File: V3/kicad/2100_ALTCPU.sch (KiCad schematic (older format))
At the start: 24 parts, among them U2100 Z8-L180-S180-180-PQFP-80, U2101 GAL16V8, X2100 14.7456 MHz

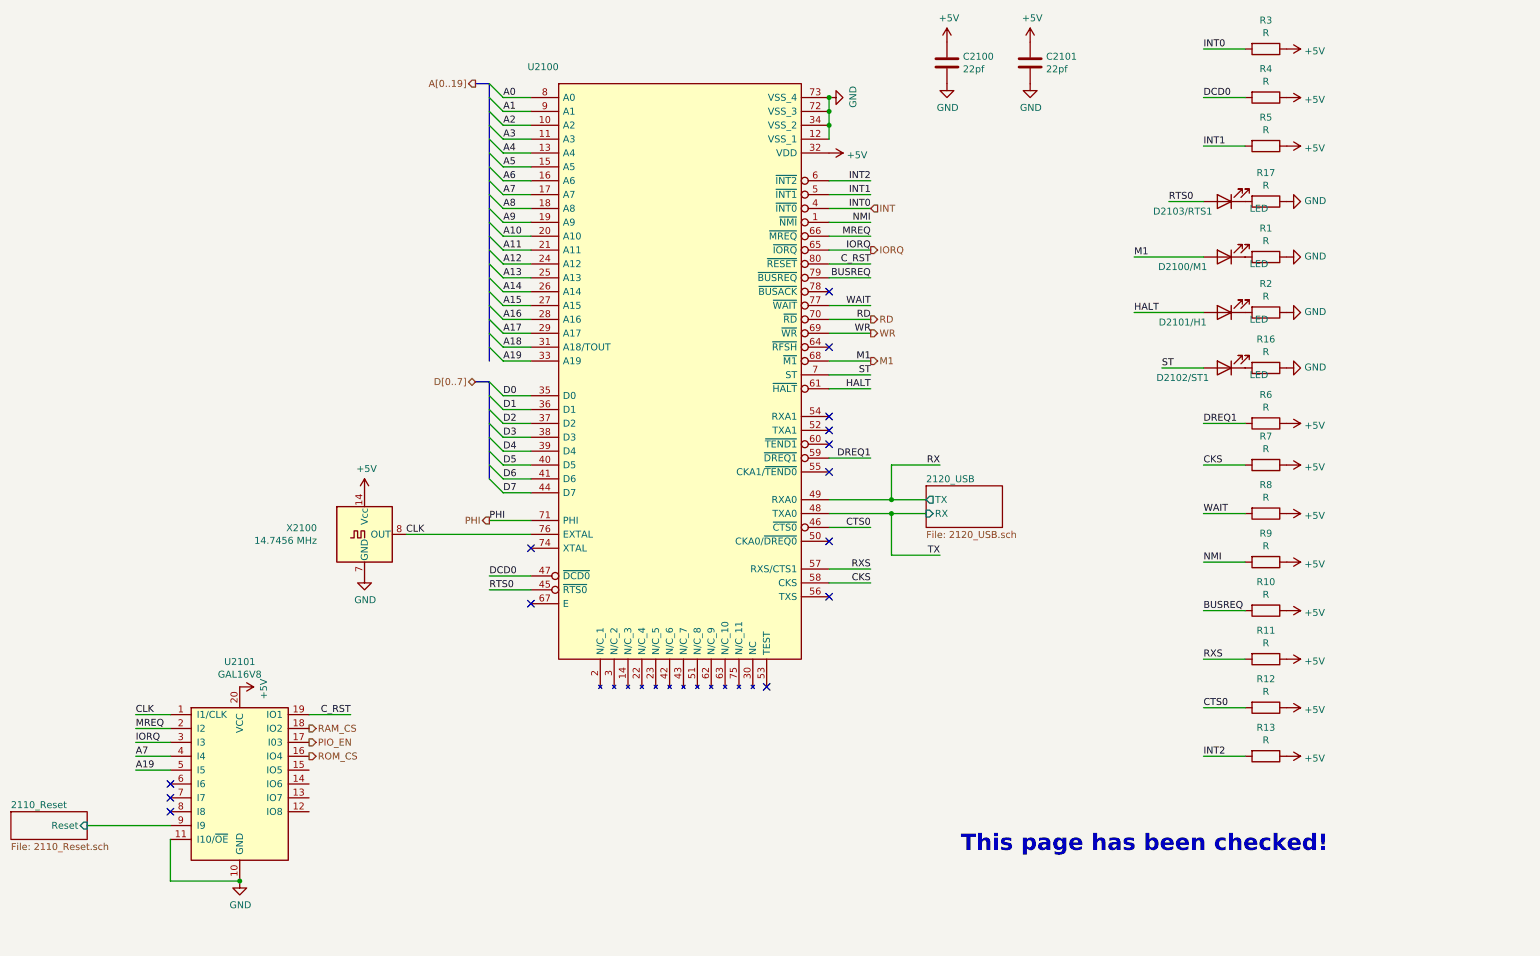
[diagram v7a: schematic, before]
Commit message: added a few caps
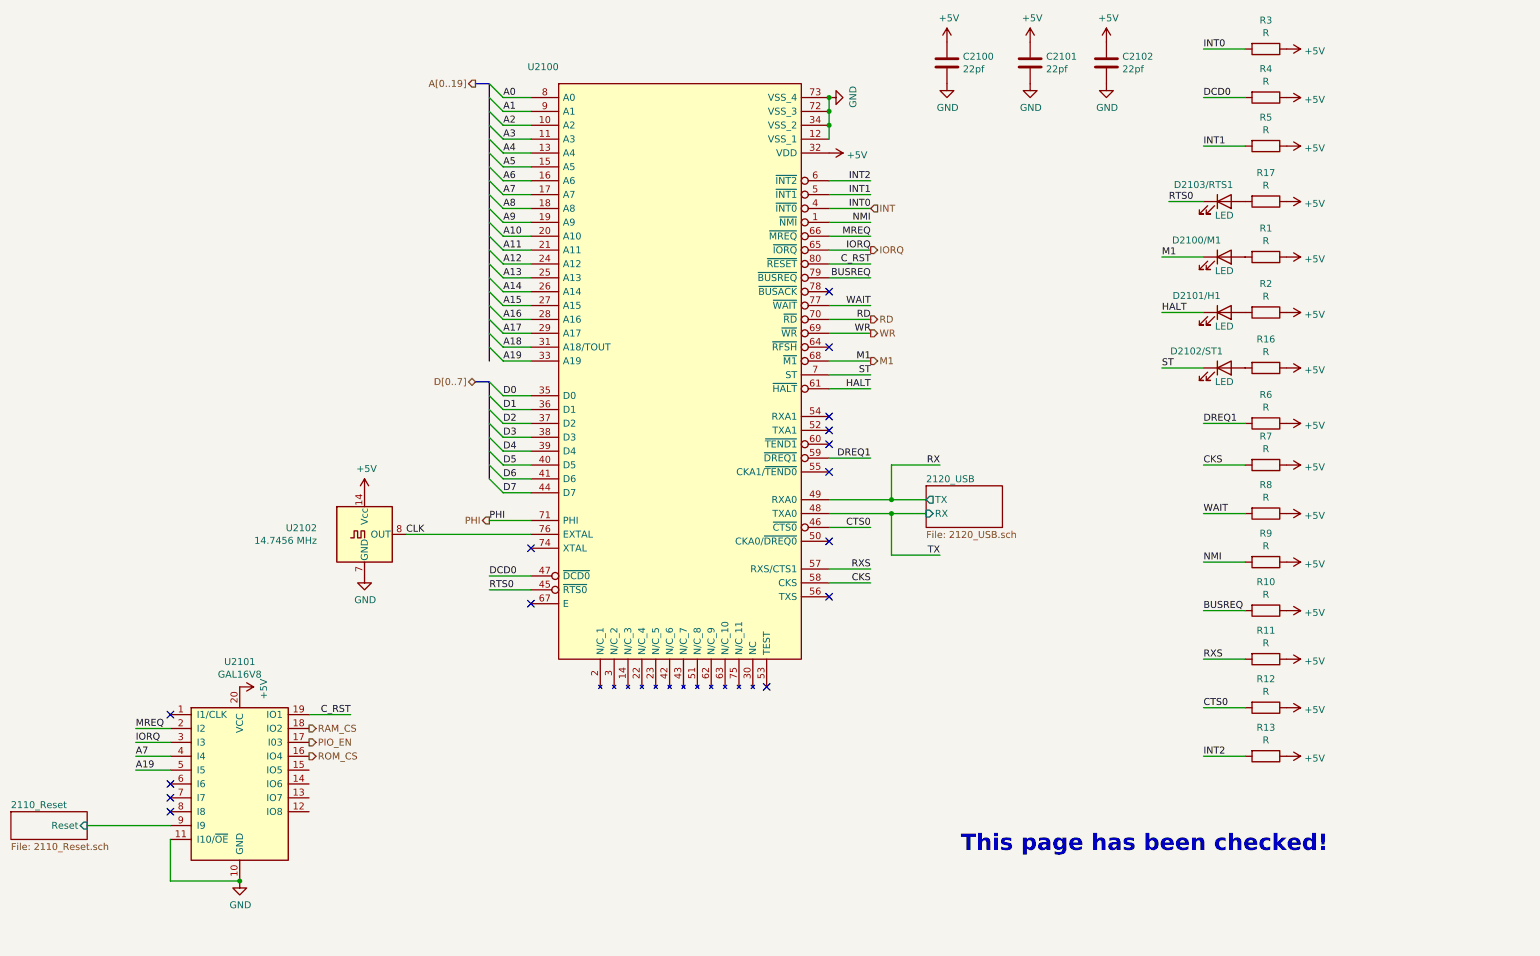
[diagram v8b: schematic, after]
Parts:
- added C2102: 22pf, Capacitor_SMD:C_1206_3216Metric, symbol Device:C
- renumbered X2100 to U2102
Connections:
- net +5V: now also R1.1, R16.1, R17.1, R2.1, C2102.1
- net CLK: no longer U2101.1 (I1/CLK)
- net GND: now also C2102.2; no longer R1.1, R16.1, R17.1, R2.1
- net HALT: now also D2101/H1.1 (K); no longer D2101/H1.2 (A)
- net M1: now also D2100/M1.1 (K); no longer D2100/M1.2 (A)
- net RTS0: now also D2103/RTS1.1 (K); no longer D2103/RTS1.2 (A)
- net ST: now also D2102/ST1.1 (K); no longer D2102/ST1.2 (A)
- net at R1.2: now also D2100/M1.2 (A); no longer D2100/M1.1 (K)
- net at R2.2: now also D2101/H1.2 (A); no longer D2101/H1.1 (K)
- net at R16.2: now also D2102/ST1.2 (A); no longer D2102/ST1.1 (K)
- net at R17.2: now also D2103/RTS1.2 (A); no longer D2103/RTS1.1 (K)
- no-connect marks 14 -> 15
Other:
- moved on the sheet: D2100/M1, D2101/H1, D2102/ST1, D2103/RTS1
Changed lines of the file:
@@
 A19
-$Comp
-L Device:LED D2100/M1
-U 1 1 6215FBC4
-P 9600 2650
-F 0 "D2100/M1" H 9900 2750 50  0000 C TNN
-F 1 "LED" H 9350 2700 50  0000 C CNN
-F 2 "LED_THT:LED_D3.0mm" H 9600 2650 50  0001 C CNN
-F 3 "~" H 9600 2650 50  0001 C CNN
-	1    9600 2650
-	-1   0    0    1
-$EndComp
 $Comp
 L power:GND #PWR?
@@
 P 3400 4650
 AR Path="/6191B6A2/6255C3DA" Ref="X?"  Part="1"
-AR Path="/6191B6A2/61EBDADB/6255C3DA" Ref="X2100"  Part="1"
-F 0 "X2100" H 3057 4696 50  0000 R CNN
+AR Path="/6191B6A2/61EBDADB/6255C3DA" Ref="U2102"  Part="1"
+F 0 "U2102" H 3057 4696 50  0000 R CNN
 F 1 "14.7456 MHz" H 3057 4605 50  0000 R CNN
 F 2 "Oscillator:Oscillator_DIP-14" H 3850 4300 50  0001 C CNN
@@
 WR
 Text Label 7050 3400 2    50   ~ 0
-M1
-Wire Wire Line
-	8950 2650 9450 2650
-Text Label 8950 2650 0    50   ~ 0
 M1
 Wire Wire Line
@@
 $EndComp
 $Comp
-L Device:LED D2101/H1
-U 1 1 62ECA51D
-P 9600 3050
-F 0 "D2101/H1" H 9900 3150 50  0000 C TNN
-F 1 "LED" H 9350 3100 50  0000 C CNN
-F 2 "LED_THT:LED_D3.0mm" H 9600 3050 50  0001 C CNN
-F 3 "~" H 9600 3050 50  0001 C CNN
-	1    9600 3050
-	-1   0    0    1
-$EndComp
-Wire Wire Line
-	8950 3050 9450 3050
-$Comp
 L Device:R R2
 U 1 1 62ECA524
@@
 	0    1    1    0
 $EndComp
-Text Label 8950 3050 0    50   ~ 0
-HALT
 $Comp
 L Device:R R6
@@
 Text Label 7050 3500 2    50   ~ 0
 ST
-Wire Wire Line
-	9450 3450 9150 3450
-Text Label 9150 3450 0    50   ~ 0
-ST
-$Comp
-L Device:LED D2102/ST1
-U 1 1 62ECE42D
-P 9600 3450
-F 0 "D2102/ST1" H 9900 3550 50  0000 C TNN
-F 1 "LED" H 9350 3500 50  0000 C CNN
-F 2 "LED_THT:LED_D3.0mm" H 9600 3450 50  0001 C CNN
-F 3 "~" H 9600 3450 50  0001 C CNN
-	1    9600 3450
-	-1   0    0    1
-$EndComp
 $Comp
 L Device:R R16
@@
 	2000 7150 2500 7150
 Connection ~ 2500 7150
-$Comp
-L power:GND #PWR0127
-U 1 1 62ED1C6A
-P 10050 2650
-F 0 "#PWR0127" H 10050 2400 50  0001 C CNN
-F 1 "GND" V 10055 2522 50  0000 R CNN
-F 2 "" H 10050 2650 50  0001 C CNN
-F 3 "" H 10050 2650 50  0001 C CNN
-	1    10050 2650
-	0    -1   -1   0
-$EndComp
-$Comp
-L power:GND #PWR0129
-U 1 1 62ED2884
-P 10050 3050
-F 0 "#PWR0129" H 10050 2800 50  0001 C CNN
-F 1 "GND" V 10055 2922 50  0000 R CNN
-F 2 "" H 10050 3050 50  0001 C CNN
-F 3 "" H 10050 3050 50  0001 C CNN
-	1    10050 3050
-	0    -1   -1   0
-$EndComp
-$Comp
-L power:GND #PWR0157
-U 1 1 62ED9834
-P 10050 3450
-F 0 "#PWR0157" H 10050 3200 50  0001 C CNN
-F 1 "GND" V 10055 3322 50  0000 R CNN
-F 2 "" H 10050 3450 50  0001 C CNN
-F 3 "" H 10050 3450 50  0001 C CNN
-	1    10050 3450
-	0    -1   -1   0
-$EndComp
 Text Label 4300 5050 0    50   ~ 0
 RTS0
@@
 U 1 1 62EF4C51
 P 9600 2250
-F 0 "D2103/RTS1" H 9900 2350 50  0000 C TNN
-F 1 "LED" H 9350 2300 50  0000 C CNN
+F 0 "D2103/RTS1" H 9450 2400 50  0000 C TNN
+F 1 "LED" H 9600 2150 50  0000 C CNN
 F 2 "LED_THT:LED_D3.0mm" H 9600 2250 50  0001 C CNN
 F 3 "~" H 9600 2250 50  0001 C CNN
 	1    9600 2250
-	-1   0    0    1
+	1    0    0    -1
 $EndComp
 $Comp
@@
 	0    1    1    0
 $EndComp
-$Comp
-L power:GND #PWR0167
-U 1 1 62EF4C5F
+NoConn ~ 2000 5950
+$Comp
+L Device:LED D2102/ST1
+U 1 1 62ECE42D
+P 9600 3450
+F 0 "D2102/ST1" H 9400 3600 50  0000 C TNN
+F 1 "LED" H 9600 3350 50  0000 C CNN
+F 2 "LED_THT:LED_D3.0mm" H 9600 3450 50  0001 C CNN
+F 3 "~" H 9600 3450 50  0001 C CNN
+	1    9600 3450
+	1    0    0    -1
+$EndComp
+Text Label 9150 3450 0    50   ~ 0
+ST
+Wire Wire Line
+	9450 3450 9150 3450
+Text Label 9150 3050 0    50   ~ 0
+HALT
+$Comp
+L Device:LED D2101/H1
+U 1 1 62ECA51D
+P 9600 3050
+F 0 "D2101/H1" H 9400 3200 50  0000 C TNN
+F 1 "LED" H 9600 2950 50  0000 C CNN
+F 2 "LED_THT:LED_D3.0mm" H 9600 3050 50  0001 C CNN
+F 3 "~" H 9600 3050 50  0001 C CNN
+	1    9600 3050
+	1    0    0    -1
+$EndComp
+Text Label 9150 2650 0    50   ~ 0
+M1
+$Comp
+L Device:LED D2100/M1
+U 1 1 6215FBC4
+P 9600 2650
+F 0 "D2100/M1" H 9400 2800 50  0000 C TNN
+F 1 "LED" H 9600 2550 50  0000 C CNN
+F 2 "LED_THT:LED_D3.0mm" H 9600 2650 50  0001 C CNN
+F 3 "~" H 9600 2650 50  0001 C CNN
+	1    9600 2650
+	1    0    0    -1
+$EndComp
+$Comp
+L power:+5V #PWR?
+U 1 1 62F15912
 P 10050 2250
-F 0 "#PWR0167" H 10050 2000 50  0001 C CNN
-F 1 "GND" V 10055 2122 50  0000 R CNN
+F 0 "#PWR?" H 10050 2100 50  0001 C CNN
+F 1 "+5V" V 10065 2378 50  0000 L CNN
 F 2 "" H 10050 2250 50  0001 C CNN
 F 3 "" H 10050 2250 50  0001 C CNN
 	1    10050 2250
-	0    -1   -1   0
-$EndComp
-Wire Wire Line
-	2000 5950 1750 5950
-Text Label 1750 5950 0    50   ~ 0
-CLK
+	0    1    1    0
+$EndComp
+$Comp
+L power:+5V #PWR?
+U 1 1 62F23F5D
+P 10050 2650
+F 0 "#PWR?" H 10050 2500 50  0001 C CNN
+F 1 "+5V" V 10065 2778 50  0000 L CNN
+F 2 "" H 10050 2650 50  0001 C CNN
+F 3 "" H 10050 2650 50  0001 C CNN
+	1    10050 2650
+	0    1    1    0
+$EndComp
+$Comp
+L power:+5V #PWR?
+U 1 1 62F23F63
+P 10050 3050
+F 0 "#PWR?" H 10050 2900 50  0001 C CNN
+F 1 "+5V" V 10065 3178 50  0000 L CNN
+F 2 "" H 10050 3050 50  0001 C CNN
+F 3 "" H 10050 3050 50  0001 C CNN
+	1    10050 3050
+	0    1    1    0
+$EndComp
+$Comp
+L power:+5V #PWR?
+U 1 1 62F330B6
+P 10050 3450
+F 0 "#PWR?" H 10050 3300 50  0001 C CNN
+F 1 "+5V" V 10065 3578 50  0000 L CNN
+F 2 "" H 10050 3450 50  0001 C CNN
+F 3 "" H 10050 3450 50  0001 C CNN
+	1    10050 3450
+	0    1    1    0
+$EndComp
+$Comp
+L Device:C C?
+U 1 1 62F37858
+P 8750 1250
+AR Path="/6195D2C9/62F37858" Ref="C?"  Part="1"
+AR Path="/6191B6A2/61F28B7D/62F37858" Ref="C?"  Part="1"
+AR Path="/6191B6A2/61EBDADB/62F37858" Ref="C2102"  Part="1"
+F 0 "C2102" H 8865 1296 50  0000 L CNN
+F 1 "22pf" H 8865 1205 50  0000 L CNN
+F 2 "Capacitor_SMD:C_1206_3216Metric" H 8788 1100 50  0001 C CNN
+F 3 "~" H 8750 1250 50  0001 C CNN
+	1    8750 1250
+	1    0    0    -1
+$EndComp
+$Comp
+L power:GND #PWR?
+U 1 1 62F3785E
+P 8750 1400
+AR Path="/62F3785E" Ref="#PWR?"  Part="1"
+AR Path="/62497D60/62F3785E" Ref="#PWR?"  Part="1"
+AR Path="/61D852D7/62F3785E" Ref="#PWR?"  Part="1"
+AR Path="/6195D2C9/62F3785E" Ref="#PWR?"  Part="1"
+AR Path="/6191B6A2/61F28B7D/62F3785E" Ref="#PWR?"  Part="1"
+AR Path="/6191B6A2/61EBDADB/62F3785E" Ref="#PWR?"  Part="1"
+F 0 "#PWR?" H 8750 1150 50  0001 C CNN
+F 1 "GND" H 8755 1227 50  0000 C CNN
+F 2 "" H 8750 1400 50  0001 C CNN
+F 3 "" H 8750 1400 50  0001 C CNN
+	1    8750 1400
+	1    0    0    -1
+$EndComp
+$Comp
+L power:+5V #PWR?
+U 1 1 62F37864
+P 8750 1100
+AR Path="/6195D2C9/62F37864" Ref="#PWR?"  Part="1"
+AR Path="/6191B6A2/61F28B7D/62F37864" Ref="#PWR?"  Part="1"
+AR Path="/6191B6A2/61EBDADB/62F37864" Ref="#PWR?"  Part="1"
+F 0 "#PWR?" H 8750 950 50  0001 C CNN
+F 1 "+5V" H 8765 1273 50  0000 C CNN
+F 2 "" H 8750 1100 50  0001 C CNN
+F 3 "" H 8750 1100 50  0001 C CNN
+	1    8750 1100
+	1    0    0    -1
+$EndComp
+Wire Wire Line
+	9150 3050 9450 3050
+Wire Wire Line
+	9150 2650 9450 2650
 Wire Bus Line
 	4300 3550 4300 4250
